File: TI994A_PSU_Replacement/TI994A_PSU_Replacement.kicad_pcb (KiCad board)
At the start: 2 copper layers, 120 x 106 mm, 18 parts, among them J1 Power In, J2 Power Out, Q1 SUP53P06-20-E3, SW1 SW_Slide_DPDT, U1 R-78CK5.0-0.5, U2 DFR0831

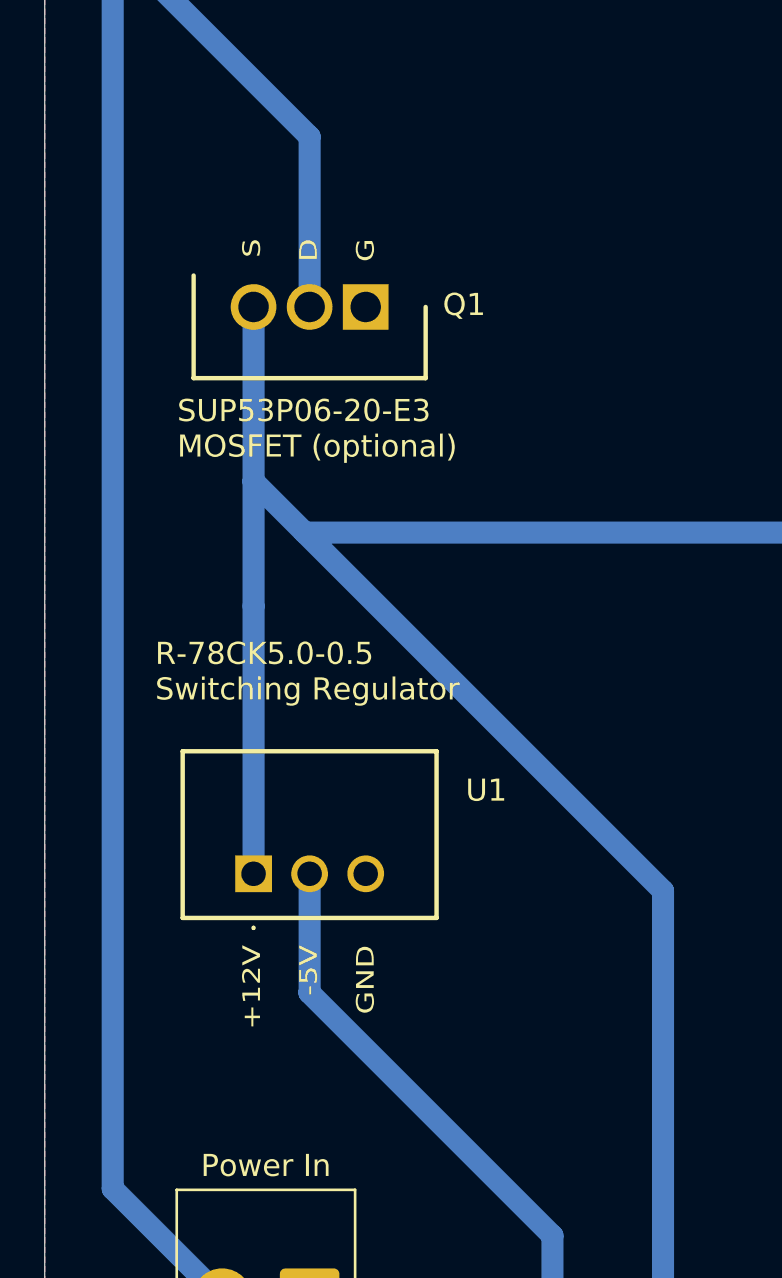
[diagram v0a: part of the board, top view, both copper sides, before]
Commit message: PCB text changes
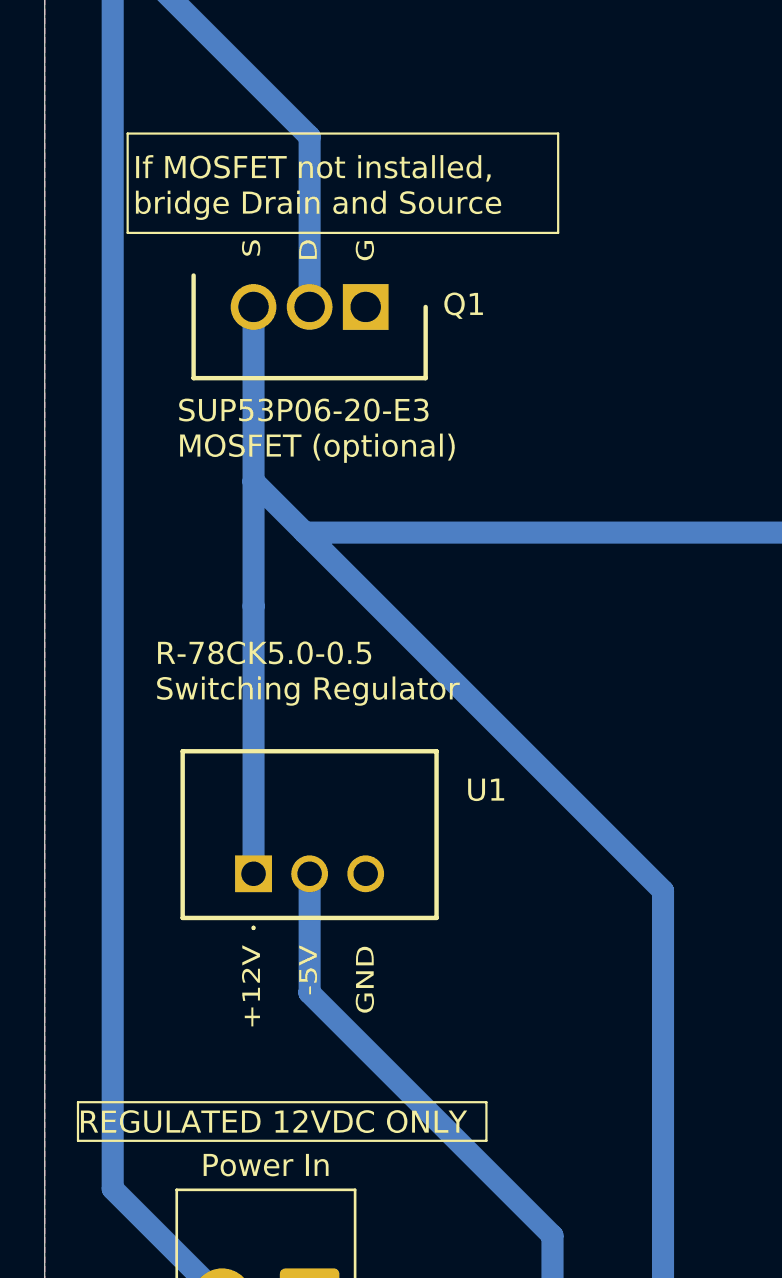
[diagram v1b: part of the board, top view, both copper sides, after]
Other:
- board text added: "If MOSFET not installed, bridge Drain and Source"
- board text added: "REGULATED 12VDC ONLY"
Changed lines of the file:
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@@
+	)
+	(gr_rect
+		(start 79.507434 115.120919)
+		(end 98.007434 116.870919)
+		(stroke
+			(width 0.1)
+			(type default)
+		)
+		(fill no)
+		(layer "F.SilkS")
+	)
+	(gr_rect
+		(start 81.757434 71.245919)
+		(end 101.257434 75.745919)
+		(stroke
+			(width 0.1)
+			(type default)
+		)
+		(fill no)
+		(layer "F.SilkS")
 	)
 	(gr_rect
@@
 				(size 1 1)
 				(thickness 0.1)
+			)
+			(justify left bottom)
+		)
+	)
+	(gr_text "REGULATED 12VDC ONLY"
+		(at 79.507434 116.620919 0)
+		(layer "F.SilkS")
+		(effects
+			(font
+				(size 1 1)
+				(thickness 0.15)
 			)
 			(justify left bottom)
@@
 		)
 	)
+	(gr_text "If MOSFET not installed,\nbridge Drain and Source"
+		(at 82.007434 74.995919 0)
+		(layer "F.SilkS")
+		(effects
+			(font
+				(size 1 1)
+				(thickness 0.15)
+			)
+			(justify left bottom)
+		)
+	)
 	(gr_text "ON  OFF"
 		(at 83.09 62.39 0)
@@
 		)
 	)
-	(gr_text_box "If MOSFET not installed,\nbridge Drain and Source"
-		(start 81.516587 70)
-		(end 102.483412 75.066349)
-		(margins 1.0025 1.0025 1.0025 1.0025)
-		(layer "F.SilkS")
-		(effects
-			(font
-				(size 1 1)
-				(thickness 0.15)
-			)
-			(justify left top)
-		)
-		(border yes)
-		(stroke
-			(width 0.2)
-			(type solid)
-		)
-	)
 	(via
 		(at 121 91)
@@
 		)
 	)
+	(group ""
+		(members "b0821140-1264-4b97-bbe2-ca57ddeada84" "b9c5666c-122f-49c9-99d1-a5a451215a29")
+	)
+	(group ""
+		(members "2f7df747-983f-40a4-9959-1a15eba39647" "497137ac-8b87-40e0-ac84-52d23925c342")
+	)
 	(embedded_fonts no)
